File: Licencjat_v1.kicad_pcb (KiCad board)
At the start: 2 copper layers, 85 x 65 mm, 73 parts, among them J1 PV_IN_1, J10 SERIAL, J2 PV_IN_2, J3 AHT20 + BMP280, J4 VEML7700, J5 ADDITIONAL I2C, J6 RF_TRANSMITTER, J7 AVR-ISP-6, J8 GEIGER, J9 1_WIRE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

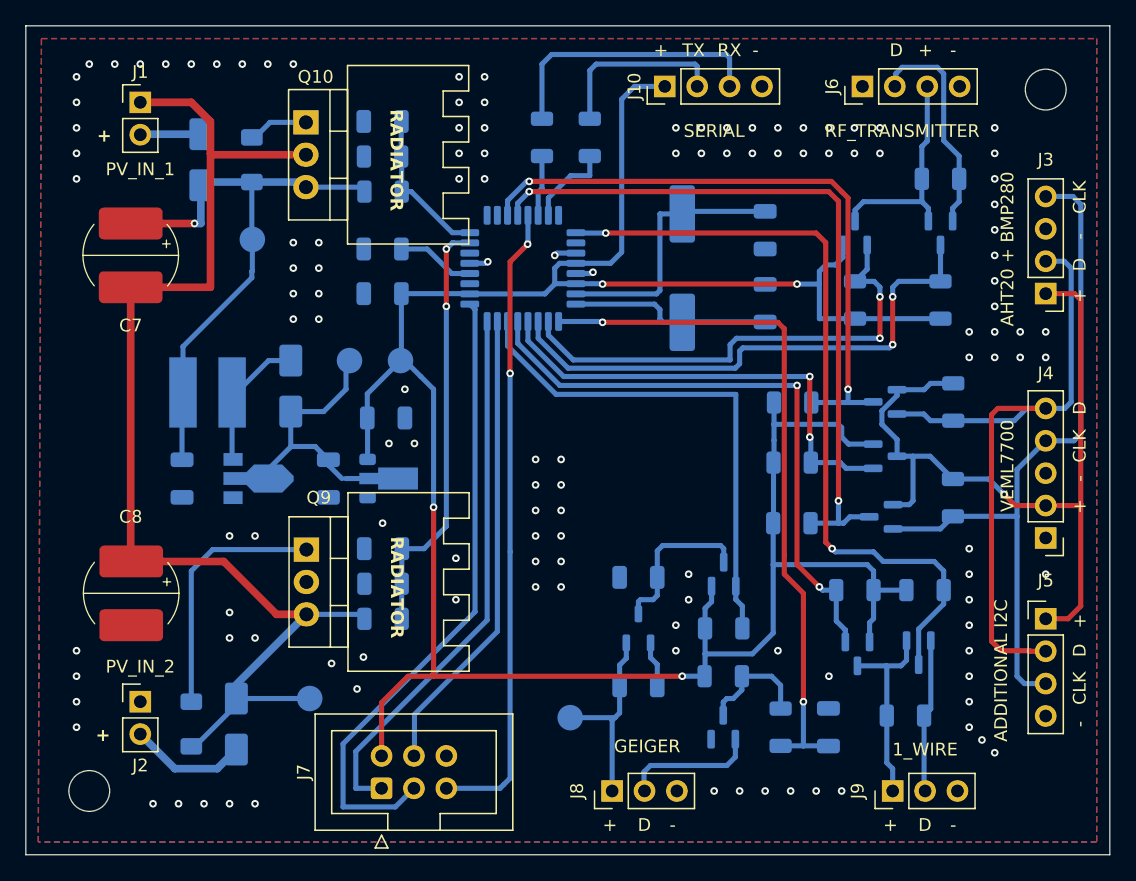
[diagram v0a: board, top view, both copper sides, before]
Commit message: Larger tracks in power section
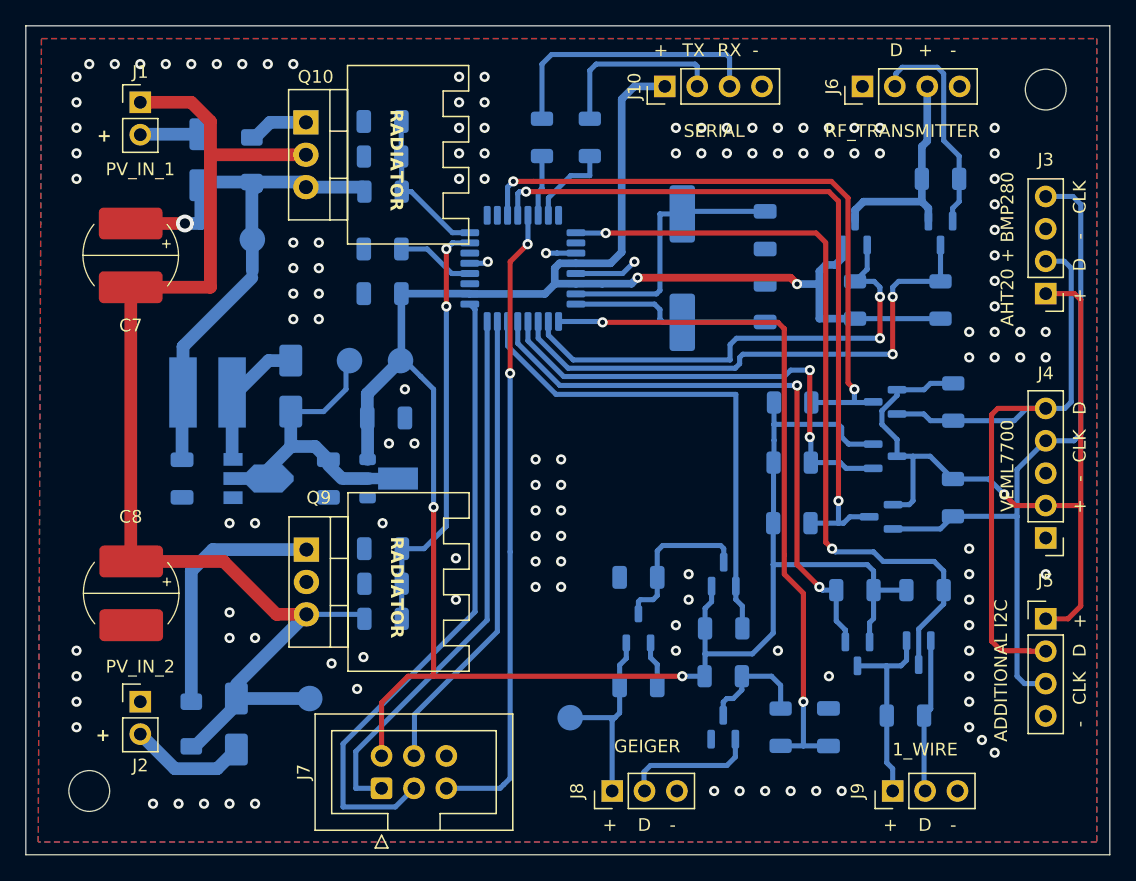
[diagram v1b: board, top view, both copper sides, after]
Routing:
- net GND: track 8.16 -> 12.4 mm
- net /SDA: track 49.9 -> 50.8 mm
- net /D8: track 36.6 -> 37.3 mm

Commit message: Add caption
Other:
- board text added: "Bezakumulatorowy czujnik klimatyczny zasilany słonecznie"
- board text added: "Daniel Wiszniowski"
- board text added: "V1.0"
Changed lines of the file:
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@@
 	)
 	(setup
+		(stackup
+			(layer "F.SilkS"
+				(type "Top Silk Screen")
+			)
+			(layer "F.Paste"
+				(type "Top Solder Paste")
+			)
+			(layer "F.Mask"
+				(type "Top Solder Mask")
+				(thickness 0.01)
+			)
+			(layer "F.Cu"
+				(type "copper")
+				(thickness 0.035)
+			)
+			(layer "dielectric 1"
+				(type "core")
+				(thickness 1.51)
+				(material "FR4")
+				(epsilon_r 4.5)
+				(loss_tangent 0.02)
+			)
+			(layer "B.Cu"
+				(type "copper")
+				(thickness 0.035)
+			)
+			(layer "B.Mask"
+				(type "Bottom Solder Mask")
+				(thickness 0.01)
+			)
+			(layer "B.Paste"
+				(type "Bottom Solder Paste")
+			)
+			(layer "B.SilkS"
+				(type "Bottom Silk Screen")
+			)
+			(copper_finish "None")
+			(dielectric_constraints no)
+		)
 		(pad_to_mask_clearance 0)
 		(allow_soldermask_bridges_in_footprints no)
@@
 		)
 		(property "Value" "1_WIRE"
-			(at 3.25 2.54 180)
+			(at 3.25 2.5 180)
 			(layer "F.SilkS")
 			(effects
@@
 		)
 		(property "Value" "ADDITIONAL I2C"
-			(at -3.5 4.06 90)
+			(at -3 3.75 90)
 			(layer "F.SilkS")
 			(effects
@@
 		)
 		(property "Value" "AHT20 + BMP280"
-			(at 3 3.5 90)
+			(at 3 4.25 90)
 			(layer "F.SilkS")
 			(effects
@@
 		)
 		(property "Value" "RF_TRANSMITTER"
-			(at -3.5 3.12 0)
+			(at -3.5 4.37 0)
 			(layer "F.SilkS")
 			(effects
@@
 		)
 		(property "Value" "GEIGER"
-			(at 3.5 2.75 180)
+			(at 3.25 2.75 180)
 			(layer "F.SilkS")
 			(effects
@@
 		(layer "Edge.Cuts")
 	)
+	(gr_text "V1.0"
+		(at 140.75 75.25 90)
+		(layer "F.SilkS")
+		(effects
+			(font
+				(size 1.5 1.5)
+				(thickness 0.3)
+				(bold yes)
+			)
+			(justify left bottom)
+		)
+	)
 	(gr_text "D"
 		(at 172.25 44.25 90)
@@
 		)
 	)
+	(gr_text "Daniel Wiszniowski"
+		(at 144.25 75.5 90)
+		(layer "F.SilkS")
+		(effects
+			(font
+				(size 1.5 1.5)
+				(thickness 0.3)
+				(bold yes)
+			)
+			(justify left bottom)
+		)
+	)
 	(gr_text "D"
 		(at 156.75 27.5 0)
@@
 			)
 			(justify left bottom)
+		)
+	)
+	(gr_text "Bezakumulatorowy \nczujnik klimatyczny \nzasilany słonecznie"
+		(at 137 75.5 90)
+		(layer "F.SilkS")
+		(effects
+			(font
+				(size 1.8 1.8)
+				(thickness 0.36)
+				(bold yes)
+			)
+			(justify left bottom)
